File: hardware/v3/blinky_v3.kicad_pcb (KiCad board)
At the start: 2 copper layers, 120 x 70 mm, 146 parts, among them J1 Conn_01x07, J2 Conn_01x03_Pin, J3 RJ45, J4 Conn_01x06_Pin, J5 Conn_01x05_Pin, J7 Conn_01x04_Pin, J8 Conn_01x04_Pin, J9 Conn_01x06_Pin, Q1 2N7002, U1 STM32F405RGTx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

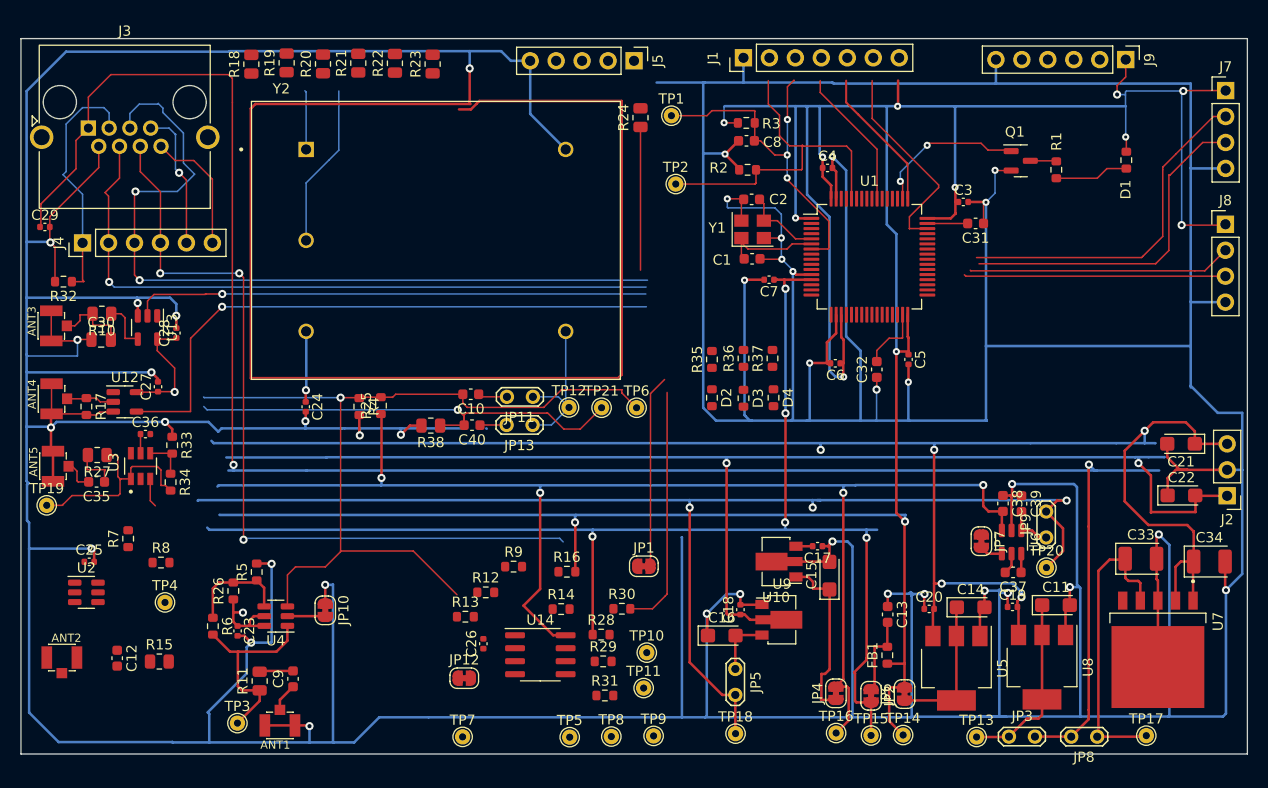
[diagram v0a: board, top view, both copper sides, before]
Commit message: update comparator and start routing
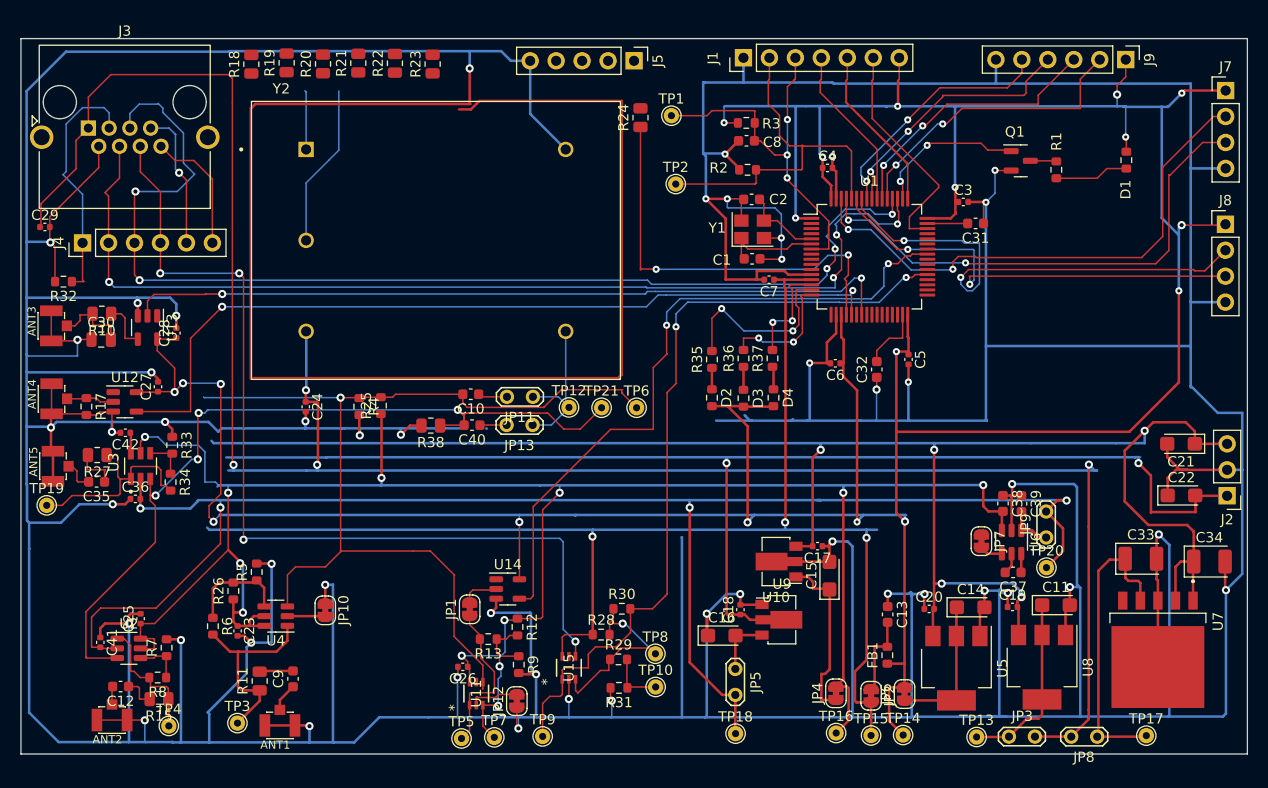
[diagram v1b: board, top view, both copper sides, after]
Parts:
- removed R14, R16: 4K7, Resistor_SMD:R_0603_1608Metric
- removed TP11: ~, TestPoint:TestPoint_THTPad_D1.5mm_Drill0.7mm
- added C41: 100nF, Capacitor_SMD:C_0402_1005Metric, F.Cu at (107.8, 109.1)
- added C42: 100nF, Capacitor_SMD:C_0402_1005Metric, F.Cu at (110.2, 88.6)
- added U11: TLV3603DCKR, blinky_footprints:SC70_DCK_TEX, F.Cu at (144.5, 114.1)
- added U15: TLV3603DCKR, blinky_footprints:SC70_DCK_TEX, F.Cu at (153.6, 111.6)
- U14: value LM393 -> SN74LVC1G14DBV; footprint Package_SO:SOIC-8_3.9x4.9mm_P1.27mm -> Package_TO_SOT_SMD:SOT-23-5
- moved JP1 17.6 mm to (143.9, 105.8), turned to 90 degrees
- moved TP4 12.1 mm to (114.5, 117.3)
- moved R7 11.3 mm to (114.2, 109.6)
- moved R8 11.3 mm to (113.4, 112.5), turned to 180 degrees
- moved TP9 10.9 mm to (151.0, 118.3)
- moved TP5 10.6 mm to (143.1, 118.5)
- moved R9 9.60 mm to (148.7, 111.3), turned to -90 degrees
- moved TP8 9.17 mm to (162.1, 110.2)
- moved ANT2 7.84 mm to (108.9, 116.7), turned to 180 degrees
- moved C25 7.50 mm to (111.7, 106.8), turned to 90 degrees
- moved U14 7.18 mm to (147.6, 103.9)
- moved U2 6.88 mm to (110.6, 109.7)
- moved C36 6.42 mm to (111.2, 95.0)
- moved JP12 5.61 mm to (148.5, 114.8), turned to 90 degrees
- moved R12 4.60 mm to (148.6, 107.6), turned to -90 degrees
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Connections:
- net Net-(JP11-A) renamed /OCXO_OUT
- net Net-(U2-+) renamed /10MHz0v
- C10 pad 2: Net-(U14B--) -> /10Mhz2.5V
- C36 pad 1: +5VA -> GND
- JP1 pad 2: EXT_CLK_IN -> Net-(JP1-B)
- R12 pad 2: Net-(U14B-+) -> Net-(U11-IN+)
- R13 pad 1: Net-(U14B-+) -> Net-(U11-IN+)
- R25 pad 2: Net-(U14B--) -> /10Mhz2.5V
- R28 pad 2: Net-(U14A-+) -> Net-(U15-IN+)
- R29 pad 1: Net-(U14A-+) -> Net-(U15-IN+)
- R30 pad 1: Net-(U14A-+) -> Net-(U15-IN+)
- R4 pad 1: Net-(U14B--) -> /10Mhz2.5V
- R9 pad 1: Net-(U14B-+) -> Net-(U11-IN+)
- TP6 pad 1: Net-(U14B--) -> /10Mhz2.5V
- TP7 pad 1: Net-(U14B-+) -> Net-(U11-IN+)
- TP8 pad 1: Net-(U14A-+) -> Net-(U15-IN+)
- U14 pad 1: GPS_PPS -> unconnected-(U14-NC-Pad1)
- U14 pad 2: Net-(J4-Pin_4) -> Net-(JP1-B)
- U14 pad 3: Net-(U14A-+) -> GND
- U14 pad 4: Net-(JP12-B) -> EXT_CLK_IN
- U14 pad 5: Net-(U14B-+) -> +3.3V
- U4 pad 3: Net-(U14B--) -> /10Mhz2.5V
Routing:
- net /10Mhz2.5V: track 0.00 -> 94.0 mm, vias 0 -> 1
- net Net-(U14B--): track 82.7 -> 0.00 mm, vias 1 -> 0
- net GPS_PPS: track 23.9 -> 77.4 mm, vias 0 -> 2
- net +5VA: track 142.5 -> 195.2 mm, vias 5 -> 10
- net +3.3V: track 309.0 -> 359.1 mm, vias 14 -> 19
- net EXT_CLK_IN: track 18.8 -> 66.0 mm, vias 0 -> 2
- net /GPS_RX1: track 66.8 -> 101.7 mm, vias 1 -> 4
- net -5VA: track 120.9 -> 154.4 mm, vias 3 -> 4
- net /GPS_TX1: track 78.1 -> 110.5 mm, vias 2 -> 5
- net /10MHz0v: track 48.0 -> 80.1 mm, vias 1 -> 4
- net /DB4: track 0.00 -> 29.5 mm, vias 0 -> 2
- net OSC_ADJ: track 14.0 -> 41.0 mm, vias 0 -> 2
- net /DB3: track 0.00 -> 26.7 mm, vias 0 -> 2
- net /DB2: track 0.00 -> 25.6 mm, vias 0 -> 2
- net SYNC_OUT: track 50.5 -> 75.9 mm, vias 1 -> 2
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
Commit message: fix errors
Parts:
- removed U11, U15: TLV3603DCKR, blinky_footprints:SC70_DCK_TEX
- added JP14: SolderJumper_2_Bridged, Jumper:SolderJumper-2_P1.3mm_Bridged_RoundedPad1.0x1.5mm, F.Cu at (106.4, 74.6)
- added R14: 130K, Resistor_SMD:R_0603_1608Metric, F.Cu at (141.3, 113.7)
- added R16: 130K, Resistor_SMD:R_0603_1608Metric, F.Cu at (151.1, 114.4)
- moved R32 1.86 mm to (102.8, 72.5), turned to -90 degrees
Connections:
- U13 pad 3: GND -> Net-(JP14-A)
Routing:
- net GND: track 1118.8 -> 1098.8 mm, vias 48 -> 49
- net Net-(JP14-A): track 0.00 -> 6.35 mm
- net Net-(U15-IN+): track 20.0 -> 13.7 mm
- net +3.3VA: track 131.3 -> 125.0 mm
- net Net-(U15-LE/HYS): track 0.00 -> 4.60 mm
- net Net-(U11-LE/HYS): track 0.00 -> 4.15 mm
- net +3.3V: track 359.1 -> 357.9 mm, vias 19 -> 17
- net /10Mhz2.5V: track 94.0 -> 93.2 mm
- net GPS_PPS: track 77.4 -> 76.8 mm

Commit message: fix most errors
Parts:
- added U11: TLV3603DCKR, blinky_footprints:SC70_DCK_TEX, F.Cu at (144.3, 114.1)
- added U15: TLV3603DCKR, blinky_footprints:SC70_DCK_TEX, F.Cu at (155.0, 112.3)
- R19, R20, R21, R22: value 49R9 -> 1K0
- moved JP7 0.73 mm to (193.2, 99.2)
- moved C34 0.65 mm to (216.3, 100.5)
- moved C36 0.53 mm to (111.2, 95.6)
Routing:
- net +15V: track 174.4 -> 113.2 mm
- net -15V: track 123.6 -> 74.7 mm
- net Net-(J5-Pin_1): track 15.9 -> 56.9 mm, vias 0 -> 1
- net +3.3VA: track 125.0 -> 93.1 mm
- net Net-(J5-Pin_3): track 5.80 -> 35.7 mm, vias 0 -> 1
- net Net-(J5-Pin_4): track 0.00 -> 26.8 mm
- net +5VA: track 195.0 -> 208.4 mm
- net /10Mhz2.5V: track 93.2 -> 81.0 mm, vias 1 -> 0
- net Net-(J5-Pin_2): track 0.00 -> 5.96 mm, vias 0 -> 1
- net Net-(R18-Pad2): track 0.00 -> 4.69 mm
- net Net-(R22-Pad2): track 0.00 -> 4.48 mm
- net Net-(R19-Pad2): track 0.00 -> 4.36 mm
- net Net-(R21-Pad2): track 0.00 -> 4.35 mm
- net Net-(U11-IN+): track 16.1 -> 18.5 mm
- net Net-(U15-IN+): track 13.7 -> 15.9 mm
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
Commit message: fix all rules
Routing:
- net GND: track 1098.7 -> 971.5 mm
- net Net-(U15-LE/HYS): track 5.21 -> 3.78 mm
- net /USB_RX: track 48.0 -> 46.7 mm
- net /GPS_RX1: track 101.7 -> 100.5 mm
- net Net-(U11-IN+): track 18.5 -> 17.3 mm
- net /USB_TX: track 43.4 -> 42.6 mm
- net /GPS_TX1: track 110.5 -> 109.8 mm
- added copper zone on B.Cu, net GND
- added copper zone on F.Cu, net GND

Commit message: update
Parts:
- added TP11: ~, TestPoint:TestPoint_THTPad_D1.5mm_Drill0.7mm, F.Cu at (107.0, 82.5)
- added TP22: ~, TestPoint:TestPoint_THTPad_D1.5mm_Drill0.7mm, F.Cu at (118.5, 82.0)
- added TP23: ~, TestPoint:TestPoint_THTPad_D1.5mm_Drill0.7mm, F.Cu at (117.0, 76.5)
- added TP24: ~, TestPoint:TestPoint_THTPad_D1.5mm_Drill0.7mm, F.Cu at (110.5, 82.0)
- moved TP10 10.8 mm to (152.0, 109.5)
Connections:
- TP10 pad 1: Net-(R29-Pad2) -> Net-(J4-Pin_4)
- TP18 pad 1: -5VA -> Net-(JP5-A)
- TP20 pad 1: -5VA -> Net-(JP9-A)
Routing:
- net -5VA: track 155.2 -> 144.6 mm
- net Net-(JP5-A): track 5.88 -> 13.5 mm
- net GND: track 971.5 -> 966.5 mm, vias 50 -> 49
- net Net-(JP9-A): track 4.57 -> 7.53 mm
- net Net-(ANT4-PadSIG): track 4.69 -> 7.63 mm
- net Net-(R29-Pad2): track 5.61 -> 2.81 mm
- net Net-(R10-Pad1): track 4.82 -> 7.62 mm
- net Net-(J4-Pin_4): track 91.8 -> 94.2 mm
- net SYNC_IN: track 81.6 -> 83.5 mm
- net SYNC_OUT: track 75.8 -> 77.3 mm
- net Net-(J5-Pin_4): track 26.8 -> 25.6 mm
- net Net-(J5-Pin_3): track 35.7 -> 34.7 mm
- net Net-(J5-Pin_1): track 56.9 -> 56.3 mm

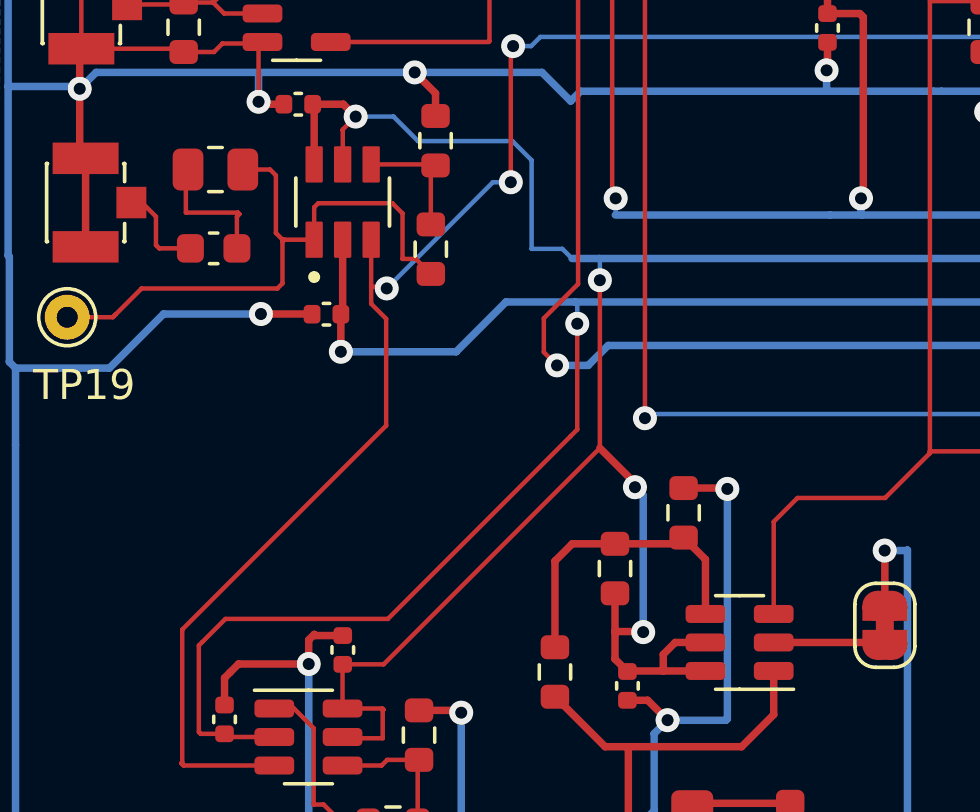
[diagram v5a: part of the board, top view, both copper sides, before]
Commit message: update op amp for single supply
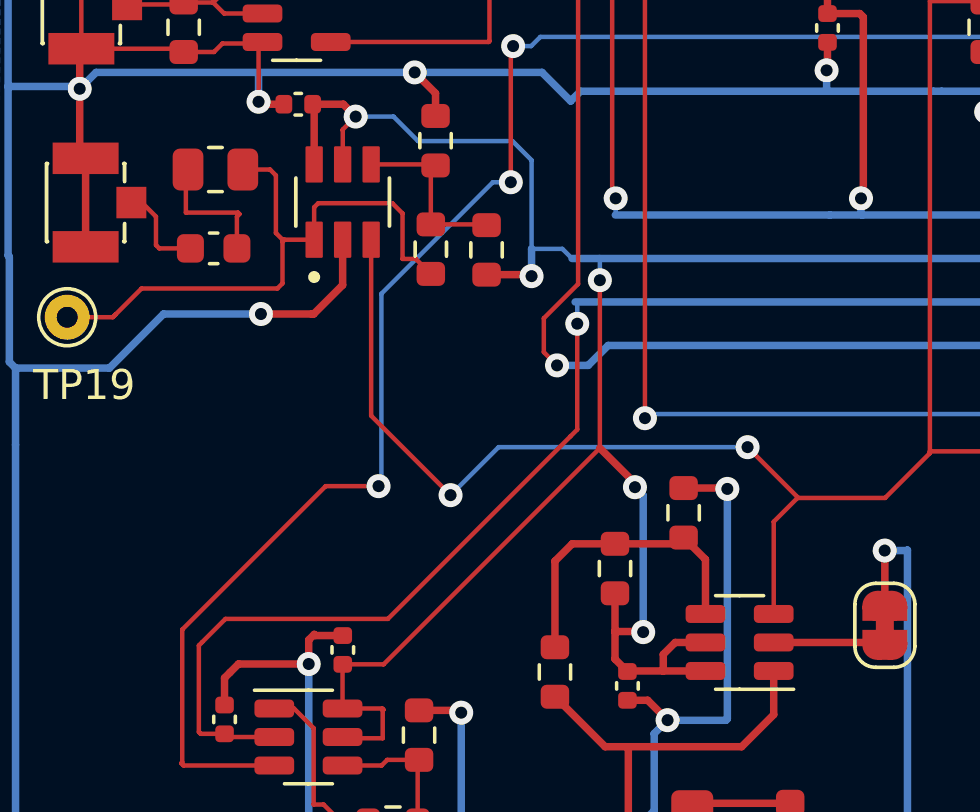
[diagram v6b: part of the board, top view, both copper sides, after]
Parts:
- removed C36: 100nF, Capacitor_SMD:C_0402_1005Metric
- added R39: 1K0, Resistor_SMD:R_0603_1608Metric, F.Cu at (116.5, 93.4)
- R33: value 510R -> 1K0
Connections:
- U3 pad 2: -5VA -> GND
- U3 pad 3: /10MHz0v -> /10Mhz2.5V
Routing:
- net /10Mhz2.5V: track 81.0 -> 103.5 mm, vias 0 -> 2
- net -5VA: track 144.6 -> 132.3 mm, vias 4 -> 3
- net GND: track 966.5 -> 969.4 mm
- net +5VA: track 208.4 -> 210.8 mm, vias 10 -> 11
- net Net-(U3--IN): track 4.19 -> 6.06 mm
- net /10MHz0v: track 80.0 -> 78.7 mm

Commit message: update
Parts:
- R10: value 200 -> 200R
- TP12, TP21, TP6: value TestPoint -> ~
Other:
- board text added: "Blinky V3.0 Cullen Jennings"
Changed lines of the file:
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@@
     (property "Sheetfile" "blinky_v3.kicad_sch")
     (property "Sheetname" "")
+    (property "dnp" "")
+    (property "exclude_from_bom" "")
     (property "ki_description" "test point")
     (property "ki_keywords" "test point tp")
-    (attr exclude_from_pos_files)
+    (attr exclude_from_pos_files exclude_from_bom)
     (fp_text reference "TP12" (at 0.025792 2.703694) (layer "F.SilkS")
         (effects (font (size 1 1) (thickness 0.15)))
     )
-    (fp_text value "TestPoint" (at 0 1.75) (layer "F.Fab") hide
+    (fp_text value "~" (at 0 1.75) (layer "F.Fab") hide
         (effects (font (size 1 1) (thickness 0.15)))
     )
@@
         (effects (font (size 1 1) (thickness 0.15)))
     )
-    (fp_text value "200" (at 0 1.65) (layer "F.Fab") hide
+    (fp_text value "200R" (at 0 1.65) (layer "F.Fab") hide
         (effects (font (size 1 1) (thickness 0.15)))
     )
@@
     (property "Sheetfile" "blinky_v3.kicad_sch")
     (property "Sheetname" "")
+    (property "dnp" "")
+    (property "exclude_from_bom" "")
     (property "ki_description" "Generic connector, single row, 01x06, script generated")
     (property "ki_keywords" "connector")
-    (attr through_hole)
+    (attr through_hole exclude_from_bom)
     (fp_text reference "J4" (at 0 -2.33 90) (layer "F.SilkS") hide
         (effects (font (size 1 1) (thickness 0.15)))
@@
     (property "Sheetfile" "blinky_v3.kicad_sch")
     (property "Sheetname" "")
+    (property "dnp" "")
+    (property "exclude_from_bom" "")
     (property "ki_description" "Generic connector, single row, 01x05, script generated")
     (property "ki_keywords" "connector")
-    (attr through_hole)
+    (attr through_hole exclude_from_bom)
     (fp_text reference "J5" (at 0 -2.33 90) (layer "F.SilkS") hide
         (effects (font (size 1 1) (thickness 0.15)))
@@
     (property "Sheetfile" "blinky_v3.kicad_sch")
     (property "Sheetname" "")
+    (property "dnp" "")
+    (property "exclude_from_bom" "")
     (property "ki_description" "test point")
     (property "ki_keywords" "test point tp")
-    (attr exclude_from_pos_files)
+    (attr exclude_from_pos_files exclude_from_bom)
     (fp_text reference "TP21" (at 1.228239 2.326754) (layer "F.SilkS")
         (effects (font (size 1 1) (thickness 0.15)))
     )
-    (fp_text value "TestPoint" (at 0 1.75) (layer "F.Fab")
+    (fp_text value "~" (at 0 1.75) (layer "F.Fab")
         (effects (font (size 1 1) (thickness 0.15)))
     )
@@
     (property "Sheetfile" "blinky_v3.kicad_sch")
     (property "Sheetname" "")
+    (property "dnp" "")
+    (property "exclude_from_bom" "")
     (property "ki_description" "test point")
     (property "ki_keywords" "test point tp")
-    (attr exclude_from_pos_files)
+    (attr exclude_from_pos_files exclude_from_bom)
     (fp_text reference "TP6" (at 0.814042 -2.162606) (layer "F.SilkS")
         (effects (font (size 1 1) (thickness 0.15)))
     )
-    (fp_text value "TestPoint" (at 0 1.75) (layer "F.Fab")
+    (fp_text value "~" (at 0 1.75) (layer "F.Fab")
         (effects (font (size 1 1) (thickness 0.15)))
     )
@@
     (property "Sheetfile" "blinky_v3.kicad_sch")
     (property "Sheetname" "")
+    (property "dnp" "")
+    (property "exclude_from_bom" "")
     (property "ki_description" "Generic connector, single row, 01x03, script generated")
     (property "ki_keywords" "connector")
-    (attr through_hole)
+    (attr through_hole exclude_from_bom)
     (fp_text reference "J2" (at 0 -2.33) (layer "F.SilkS") hide
         (effects (font (size 1 1) (thickness 0.15)))
@@
   (gr_line (start 100 50) (end 100 120)
     (stroke (width 0.1) (type default)) (layer "Edge.Cuts"))
+  (gr_text "Blinky V3.0	\nCullen Jennings" (at 196.6 84.7) (layer "F.SilkS")
+    (effects (font (size 1 1) (thickness 0.15)) (justify left bottom))
+  )
   (segment (start 181.811009 84.414379) (end 181.811009 97.298234) (width 0.25) (layer "F.Cu") (net 1))
   (segment (start 185.537894 81.533456) (end 185.537894 88.358062) (width 0.25) (layer "F.Cu") (net 1))
